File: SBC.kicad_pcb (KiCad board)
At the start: 4 copper layers, 85 x 54 mm, 283 parts, among them J1 USB_OTG, J2 DIN41612_02x10_AB, J3 USB_OTG, J4 Conn_02x20_Counter_Clockwise, J5 Conn_01x15_Socket, J6 Conn_01x06_Socket, SW1 SW_DIP_x03, U1 STPMIC1APQR, U2 IS43TR16640C-125JBL, U3 ECMF02-2AMX6, U4 ECMF02-2AMX6, U5 STM32MP157FADx, U6 IS21ES08GA-JQLI-TR, U7 LAN8720A, U8 ARJM11C7-114-BA-EW2, X1 ASE-24MHz, Y1 25MHz

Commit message: Layout started
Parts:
- removed R17: 680, Resistor_SMD:R_0402_1005Metric
- removed R18, R19, R20: 22, Resistor_SMD:R_0402_1005Metric
- removed R21, R22: 10k, Resistor_SMD:R_0402_1005Metric
- removed R23, R24: 1.5k, Resistor_SMD:R_0402_1005Metric
- removed R25: 3k, Resistor_SMD:R_0402_1005Metric
- added D10: Red, SparkFun-LED:LED_0603_1608Metric, F.Cu at (178.4, 70.3)
- added D11: Red, SparkFun-LED:LED_0603_1608Metric, F.Cu at (178.4, 72.8)
- added D12: Red, SparkFun-LED:LED_0603_1608Metric, F.Cu at (178.4, 75.3)
- added D13: Red, SparkFun-LED:LED_0603_1608Metric, F.Cu at (178.4, 77.8)
- added D14: Red, SparkFun-LED:LED_0603_1608Metric, F.Cu at (178.4, 80.3)
- added D15: Red, SparkFun-LED:LED_0603_1608Metric, F.Cu at (193.2, 76.4)
- added D16: Blue, SparkFun-LED:LED_0603_1608Metric, F.Cu at (193.2, 78.9)
- added D17: ECMF04-4HSWM10, footprints:QFN-10L_DTS, F.Cu at (106.0, 80.0)
- added D18: ECMF04-4HSWM10, footprints:QFN-10L_DTS, F.Cu at (197.5, 73.0)
- added D5: Red, SparkFun-LED:LED_0603_1608Metric, F.Cu at (53.0, 33.8)
- added D6: Red, SparkFun-LED:LED_0603_1608Metric, F.Cu at (178.4, 60.3)
- added D7: Red, SparkFun-LED:LED_0603_1608Metric, F.Cu at (178.4, 62.8)
- added D8: Red, SparkFun-LED:LED_0603_1608Metric, F.Cu at (178.4, 65.3)
- added D9: Red, SparkFun-LED:LED_0603_1608Metric, F.Cu at (178.4, 67.8)
- added R10: 680, Resistor_SMD:R_0402_1005Metric, F.Cu at (187.7, 62.0)
- added R11: 680, Resistor_SMD:R_0402_1005Metric, F.Cu at (187.7, 64.0)
- added R129: 75, Capacitor_SMD:C_0402_1005Metric, F.Cu at (52.5, 36.0)
- added R130: 75, Capacitor_SMD:C_0402_1005Metric, F.Cu at (192.6, 60.0)
- added R131: 75, Capacitor_SMD:C_0402_1005Metric, F.Cu at (192.6, 62.0)
- added R132: 75, Capacitor_SMD:C_0402_1005Metric, F.Cu at (192.6, 63.9)
- added R133: 4.75k, Capacitor_SMD:C_0402_1005Metric, F.Cu at (192.6, 65.9)
- added R134: 4.75k, Capacitor_SMD:C_0402_1005Metric, F.Cu at (192.6, 67.9)
- added R135: 4.75k, Capacitor_SMD:C_0402_1005Metric, F.Cu at (195.5, 60.0)
- added R136: 4.75k, Capacitor_SMD:C_0402_1005Metric, F.Cu at (195.5, 62.0)
- added R137: 4.75k, Capacitor_SMD:C_0402_1005Metric, F.Cu at (195.5, 63.9)
- added R138: 0, Capacitor_SMD:C_0402_1005Metric, F.Cu at (195.5, 65.9)
- added R139: 4.75k, Capacitor_SMD:C_0402_1005Metric, F.Cu at (195.5, 67.9)
- added R140: 4.75k, Capacitor_SMD:C_0402_1005Metric, F.Cu at (198.4, 60.0)
- added R141: 4.75k, Capacitor_SMD:C_0402_1005Metric, F.Cu at (198.4, 62.0)
- added R142: 4.75k, Capacitor_SMD:C_0402_1005Metric, F.Cu at (198.4, 63.9)
- added R3: 680, Resistor_SMD:R_0402_1005Metric, F.Cu at (181.9, 60.0)
- added R4: 680, Resistor_SMD:R_0402_1005Metric, F.Cu at (181.9, 62.0)
- added R5: 680, Resistor_SMD:R_0402_1005Metric, F.Cu at (181.9, 64.0)
- added R6: 680, Resistor_SMD:R_0402_1005Metric, F.Cu at (184.8, 60.0)
- added R7: 680, Resistor_SMD:R_0402_1005Metric, F.Cu at (184.8, 62.0)
- added R8: 680, Resistor_SMD:R_0402_1005Metric, F.Cu at (184.8, 64.0)
- added R9: 680, Resistor_SMD:R_0402_1005Metric, F.Cu at (187.7, 60.0)
- D2: value Blue -> Red
- D3, D4: value ECMF04-4HSWM10 -> Red; footprint footprints:QFN-10L_DTS -> SparkFun-LED:LED_0603_1608Metric
- R1, R2: value 1.5k -> 680; footprint SparkFun-Resistor:R_0603_1608Metric -> Resistor_SMD:R_0402_1005Metric
- R101, R102, R103, R114: footprint Capacitor_SMD:C_0402_1005Metric -> Resistor_SMD:R_0402_1005Metric
- R104, R105, R106, R107: value 49.9 -> 10k; footprint Capacitor_SMD:C_0402_1005Metric -> Resistor_SMD:R_0402_1005Metric
- R108, R109: value 270 -> 10k; footprint Capacitor_SMD:C_0402_1005Metric -> Resistor_SMD:R_0402_1005Metric
- R110: value 12.1k -> 10k; footprint Capacitor_SMD:C_0402_1005Metric -> Resistor_SMD:R_0402_1005Metric
- R111, R112, R113: value 0 -> 10k; footprint Capacitor_SMD:C_0402_1005Metric -> Resistor_SMD:R_0402_1005Metric
- R115, R116, R117: value 75 -> 10k
- R118: value 75 -> 49.9
- R119, R120, R121: value 4.75k -> 49.9
- R12: value 240 -> 1.5k; footprint Resistor_SMD:R_0402_1005Metric -> SparkFun-Resistor:R_0603_1608Metric
- R122, R123: value 4.75k -> 270
- R124: value 0 -> 12.1k
- R125, R126, R127: value 4.75k -> 0
- R128: value 4.75k -> 10k
- R13: value 100 -> 1.5k; footprint Resistor_SMD:R_0402_1005Metric -> SparkFun-Resistor:R_0603_1608Metric
- R14: value 1k -> 680
- R15: value 22 -> 680
- R26, R50: value 10k -> 240
- R27: value 22 -> 100
- R28: value 10 -> 1k
- R29, R32: value 0 -> 22
- R30: value 10k -> 680
- R31: value 0 -> 680
- R33: value 1k -> 22
- R34, R41: value 10k -> 22
- R36: value 240 -> 10k
- R37, R38: value 10k -> 1.5k
- R39: value 10k -> 3k
- R42: value 10k -> 10
- R43, R45, R46: value 10k -> 0
- R47: value 10k -> 1k
- moved U3 211.9 mm to (40.0, 50.5), turned to 180 degrees
- moved U4 210.6 mm to (40.0, 61.5), turned to 180 degrees
- moved U6 206.3 mm to (63.5, 66.0)
- moved SW2 198.8 mm to (55.5, 44.0)
- moved U2 187.9 mm to (79.2, 57.6), turned to -90 degrees
- moved J1 184.9 mm to (33.0, 51.0), turned to -90 degrees
- moved J3 184.4 mm to (33.0, 62.0), turned to -90 degrees
- moved U7 172.5 mm to (58.0, 84.0), turned to 90 degrees
- moved U1 172.5 mm to (79.5, 85.0)
- moved X1 166.0 mm to (89.0, 73.5)
- moved U8 163.1 mm to (46.5, 89.2), turned to 90 degrees
- moved U5 162.0 mm to (79.2, 71.0), turned to 90 degrees
- moved J6 154.3 mm to (99.2, 49.5), turned to 90 degrees
- moved J4 141.7 mm to (63.6, 45.0), turned to 90 degrees
- moved J5 137.9 mm to (107.9, 66.0), turned to 90 degrees
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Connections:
- D1 pad 2: VDD -> VIN
- D2 pad 2: VDD -> /MPU/VDDCORE
- D3 pad 1: Net-(J5-Pin_6) -> Net-(D3-K)
- D3 pad 2: Net-(J5-Pin_5) -> /MPU/VDD_DDR
- D4 pad 1: Net-(D4-D1+-Pad1) -> Net-(D4-K)
- D4 pad 2: Net-(D4-D1+-Pad1) -> VDD
- J4 pad 1: /MPU/PA3 -> VIN
- J4 pad 11: /MPU/PB12 -> GND
- J4 pad 20: /MPU/PC10 -> GND
- J4 pad 21: /MPU/PC11 -> GND
- J4 pad 30: /MPU/PD5 -> GND
- J4 pad 39: /MPU/PE0 -> GND
- J4 pad 40: /MPU/PE1 -> VIN
- R1 pad 1: /Power/VIO -> Net-(D1-K)
- R1 pad 2: /MPU/I2C_SCL -> GND
- R100 pad 1: /MPU/PD7 -> /MPU/PC8
- R101 pad 1: /NAND/VDD -> /MPU/PC9
- R101 pad 2: /MPU/SDMMC2_CMD -> GND
- R102 pad 1: /NAND/VDD -> /MPU/PC10
- R102 pad 2: /MPU/SDMMC2_CLK -> GND
- R103 pad 1: /NAND/VDD -> /MPU/PC11
- R103 pad 2: /MPU/SDMMC2_D0 -> GND
- R104 pad 1: /Ethernet/RXN -> /MPU/PC12
- R104 pad 2: /Ethernet/VDDA -> GND
- R105 pad 1: /Ethernet/RXP -> /MPU/PC13
- R105 pad 2: /Ethernet/VDDA -> GND
- R106 pad 1: /Ethernet/TXN -> /MPU/PC14
- R106 pad 2: /Ethernet/VDDA -> GND
- R107 pad 1: /Ethernet/TXP -> /MPU/PC15
- R107 pad 2: /Ethernet/VDDA -> GND
- R108 pad 1: GND -> /MPU/PD0
- R108 pad 2: /Ethernet/GREEN -> GND
- R109 pad 1: GND -> /MPU/PD1
- R109 pad 2: /Ethernet/YELLOW -> GND
- R110 pad 1: Net-(U7-RBIAS) -> /MPU/PD2
- R111 pad 1: /Ethernet/ETH_CLK -> /MPU/PD4
- R111 pad 2: Net-(U7-XTAL1/CLKIN) -> GND
- R112 pad 1: Net-(C73-Pad2) -> /MPU/PD5
- R112 pad 2: /Ethernet/ETH_CLK -> GND
- R113 pad 1: Net-(U7-XTAL2) -> /MPU/PD6
- R113 pad 2: Net-(C74-Pad2) -> GND
- R114 pad 1: /Ethernet/LED2 -> /MPU/PD7
- R115 pad 1: Net-(C76-Pad1) -> /NAND/VDD
- R115 pad 2: Net-(U8-VC2-) -> /MPU/SDMMC2_CMD
- R116 pad 1: Net-(C77-Pad1) -> /NAND/VDD
- R116 pad 2: Net-(U8-VC1-) -> /MPU/SDMMC2_CLK
- R117 pad 1: Net-(C78-Pad1) -> /NAND/VDD
- R117 pad 2: Net-(U8-VC2+) -> /MPU/SDMMC2_D0
- R118 pad 1: Net-(C79-Pad1) -> /Ethernet/RXN
- R118 pad 2: Net-(U8-VC1+) -> /Ethernet/VDDA
- R119 pad 1: /Ethernet/PHYADDR -> /Ethernet/RXP
- R119 pad 2: VDD -> /Ethernet/VDDA
- R12 pad 1: /Memory/ZQ -> /Power/VIO
- R12 pad 2: GND -> /MPU/I2C_SCL
- R120 pad 1: /Ethernet/MODE0 -> /Ethernet/TXN
- R120 pad 2: VDD -> /Ethernet/VDDA
- R121 pad 1: /Ethernet/MODE1 -> /Ethernet/TXP
- R121 pad 2: VDD -> /Ethernet/VDDA
- R122 pad 1: /Ethernet/MODE2 -> GND
- R122 pad 2: VDD -> /Ethernet/GREEN
- R123 pad 1: /MPU/ETH1_RMII_REF_CLK -> GND
- R123 pad 2: VDD -> /Ethernet/YELLOW
- R124 pad 1: /Ethernet/REFCLKO -> Net-(U7-RBIAS)
- R124 pad 2: /MPU/ETH1_RMII_REF_CLK -> GND
- R125 pad 1: GND -> /Ethernet/ETH_CLK
- R125 pad 2: /Ethernet/PHYADDR -> Net-(U7-XTAL1/CLKIN)
- R126 pad 1: GND -> Net-(C73-Pad2)
- R126 pad 2: /Ethernet/MODE0 -> /Ethernet/ETH_CLK
- R127 pad 1: GND -> Net-(U7-XTAL2)
- R127 pad 2: /Ethernet/MODE1 -> Net-(C74-Pad2)
- R128 pad 1: GND -> /Ethernet/LED2
- R128 pad 2: /Ethernet/MODE2 -> GND
- R13 pad 1: /MPU/DDR_CLKP -> /Power/VIO
- R13 pad 2: /MPU/DDR_CLKN -> /MPU/I2C_SDA
- R14 pad 1: VDD -> Net-(D12-K)
- R14 pad 2: Net-(R14-Pad2) -> GND
- R15 pad 1: /MPU/ETH_CLK_R -> Net-(D13-K)
- R15 pad 2: /Ethernet/ETH_CLK -> GND
- R16 pad 1: /MPU/DBGRQ -> Net-(D14-K)
- R16 pad 2: Net-(D2-K) -> GND
- R2 pad 1: /Power/VIO -> Net-(D2-K)
- R2 pad 2: /MPU/I2C_SDA -> GND
- R26 pad 1: GND -> /Memory/ZQ
- R26 pad 2: Net-(J2-Pin_a6) -> GND
- R27 pad 1: /MPU/ETH1_MDC_R -> /MPU/DDR_CLKP
- R27 pad 2: /Ethernet/MDC -> /MPU/DDR_CLKN
- R28 pad 2: Net-(X1-Vdd) -> Net-(R28-Pad2)
- R29 pad 1: Net-(U5-DDR_DTO1) -> /MPU/ETH_CLK_R
- R29 pad 2: GND -> /Ethernet/ETH_CLK
- R30 pad 1: VDD -> /MPU/DBGRQ
- R30 pad 2: Net-(X1-EN) -> Net-(D16-K)
- R31 pad 1: Net-(U5-DDR_DTO0) -> /MPU/DBGACK
- R31 pad 2: GND -> Net-(D15-K)
- R32 pad 1: /MPU/OSC_OUT -> /MPU/ETH1_RMII_TX_EN_R
- R32 pad 2: Net-(X1-EN) -> /Ethernet/TXEN
- R33 pad 1: GND -> /MPU/ETH1_RMII_TXD1_R
- R33 pad 2: /MPU/OSC_OUT -> /Ethernet/TXD1
- R34 pad 1: /MPU/DDR_RESETn -> /MPU/ETH1_RMII_TXD0_R
- R34 pad 2: GND -> /Ethernet/TXD0
- R35 pad 1: /MPU/DDR_CKE -> GND
- R35 pad 2: GND -> /MPU/DBGACK
- R36 pad 1: /MPU/ZQ -> GND
- R36 pad 2: GND -> /MPU/DBGRQ
- R37 pad 1: Net-(D4-D1+-Pad10) -> /Ethernet/MDC
- R37 pad 2: GND -> VDD
- R38 pad 1: Net-(D4-D1+-Pad1) -> /MPU/ETH1_MDIO
- R38 pad 2: GND -> VDD
- R39 pad 1: /MPU/PD8 -> /MPU/USB_RREF
- R40 pad 1: /MPU/PD9 -> GND
- R40 pad 2: GND -> Net-(J2-Pin_a6)
- R41 pad 1: /MPU/PD10 -> /MPU/ETH1_MDC_R
- R41 pad 2: GND -> /Ethernet/MDC
- R42 pad 1: /MPU/PD11 -> VDD
- R42 pad 2: GND -> Net-(X1-Vdd)
- R43 pad 1: /MPU/PD14 -> Net-(U5-DDR_DTO1)
- R44 pad 1: /MPU/PD15 -> VDD
- R44 pad 2: GND -> Net-(X1-EN)
- R45 pad 1: /MPU/PE0 -> Net-(U5-DDR_DTO0)
- R46 pad 1: /MPU/PE1 -> /MPU/OSC_OUT
- R46 pad 2: GND -> Net-(X1-EN)
- R47 pad 1: /MPU/PE2 -> GND
- R47 pad 2: GND -> /MPU/OSC_OUT
- R48 pad 1: /MPU/PE4 -> /MPU/DDR_RESETn
- R49 pad 1: /MPU/PE6 -> /MPU/DDR_CKE
- R50 pad 1: /MPU/PE7 -> /MPU/ZQ
- R51 pad 1: /MPU/PE8 -> Net-(D18-D1+-Pad10)
- R52 pad 1: /MPU/PE9 -> Net-(D18-D1+-Pad1)
- R53 pad 1: /MPU/PE10 -> /MPU/PD8
- R54 pad 1: /MPU/PE11 -> /MPU/PD9
- R55 pad 1: /MPU/PE12 -> /MPU/PD10
- R56 pad 1: /MPU/PE13 -> /MPU/PD11
- R57 pad 1: /MPU/PE14 -> /MPU/PD14
- R58 pad 1: /MPU/PE15 -> /MPU/PD15
- R59 pad 1: /MPU/PF6 -> /MPU/PE0
- R60 pad 1: /MPU/PF7 -> /MPU/PE1
- R61 pad 1: /MPU/PF8 -> /MPU/PE2
- R62 pad 1: /MPU/PF9 -> /MPU/PE4
- R63 pad 1: /MPU/PF10 -> /MPU/PE6
- R64 pad 1: /MPU/PF11 -> /MPU/PE7
- R65 pad 1: /MPU/PG7 -> /MPU/PE8
- R66 pad 1: /MPU/PG9 -> /MPU/PE9
- R67 pad 1: /MPU/PG10 -> /MPU/PE10
- R68 pad 1: /MPU/PG15 -> /MPU/PE11
- R69 pad 1: /MPU/PA3 -> /MPU/PE12
- R70 pad 1: /MPU/PA4 -> /MPU/PE13
- R71 pad 1: /MPU/PA5 -> /MPU/PE14
- R72 pad 1: /MPU/PA6 -> /MPU/PE15
- R73 pad 1: /MPU/PA8 -> /MPU/PF6
- R74 pad 1: /MPU/PA9 -> /MPU/PF7
- R75 pad 1: /MPU/PB1 -> /MPU/PF8
- R76 pad 1: /MPU/PB5 -> /MPU/PF9
- R77 pad 1: /MPU/PB6 -> /MPU/PF10
- R78 pad 1: /MPU/PB7 -> /MPU/PF11
- R79 pad 1: /MPU/PB12 -> /MPU/PG7
- R80 pad 1: /MPU/PB13 -> /MPU/PG9
- R81 pad 1: /MPU/PC0 -> /MPU/PG10
- R82 pad 1: /MPU/PC2 -> /MPU/PG15
- R83 pad 1: /MPU/PC3 -> /MPU/PA3
- R84 pad 1: /MPU/PC6 -> /MPU/PA4
- R85 pad 1: /MPU/PC7 -> /MPU/PA5
- R86 pad 1: /MPU/PC8 -> /MPU/PA6
- R87 pad 1: /MPU/PC9 -> /MPU/PA8
- R88 pad 1: /MPU/PC10 -> /MPU/PA9
- R89 pad 1: /MPU/PC11 -> /MPU/PB1
- R90 pad 1: /MPU/PC12 -> /MPU/PB5
- R91 pad 1: /MPU/PC13 -> /MPU/PB6
- R92 pad 1: /MPU/PC14 -> /MPU/PB7
- R93 pad 1: /MPU/PC15 -> /MPU/PB12
- R94 pad 1: /MPU/PD0 -> /MPU/PB13
- R95 pad 1: /MPU/PD1 -> /MPU/PC0
- R96 pad 1: /MPU/PD2 -> /MPU/PC2
- R97 pad 1: /MPU/PD4 -> /MPU/PC3
- R98 pad 1: /MPU/PD5 -> /MPU/PC6
- R99 pad 1: /MPU/PD6 -> /MPU/PC7
- SW1 pad 4: Net-(R14-Pad2) -> Net-(R28-Pad2)
- SW1 pad 5: Net-(R14-Pad2) -> Net-(R28-Pad2)
- SW1 pad 6: Net-(R14-Pad2) -> Net-(R28-Pad2)
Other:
- board size 85 x 54 mm -> 85 x 73 mm
- copper layers 4 -> 6

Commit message: Component placement
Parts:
- removed SW2: ~, SparkFun-Switch:Push_SMD_4.2x3.2mm
- added H1: MountingHole, MountingHole:MountingHole_3.2mm_M3, F.Cu at (34.0, 44.0)
- added H2: MountingHole, MountingHole:MountingHole_3.2mm_M3, F.Cu at (34.0, 90.0)
- added H3: MountingHole, MountingHole:MountingHole_3.2mm_M3, F.Cu at (111.0, 44.0)
- added H4: MountingHole, MountingHole:MountingHole_3.2mm_M3, F.Cu at (111.0, 90.0)
- added JP1: SolderJumper_2_Open, SparkFun-Jumper:Jumper_2_NO, F.Cu at (111.0, 76.5)
- added JP2: SolderJumper_2_Open, SparkFun-Jumper:Jumper_2_NO, F.Cu at (111.0, 78.9)
- added JP3: SolderJumper_2_Open, SparkFun-Jumper:Jumper_2_NO, F.Cu at (111.0, 81.4)
- added R143: 4.75k, Capacitor_SMD:C_0402_1005Metric, F.Cu at (120.3, 82.8)
- added R144: 4.75k, Capacitor_SMD:C_0402_1005Metric, F.Cu at (120.3, 84.8)
- added TP22: RCWCTE, footprints:TP420X150, F.Cu at (94.0, 92.0)
- added TP23: RCWCTE, footprints:TP420X150, F.Cu at (101.5, 92.0)
- R115, R116: footprint Capacitor_SMD:C_0402_1005Metric -> Resistor_SMD:R_0402_1005Metric
- R118, R119: value 49.9 -> 10k
- R12: footprint SparkFun-Resistor:R_0603_1608Metric -> Resistor_SMD:R_0402_1005Metric
- R122, R123: value 270 -> 49.9
- R124: value 12.1k -> 270
- R125: value 0 -> 270
- R126: value 0 -> 12.1k
- R128, R48: value 10k -> 0
- R129: value 75 -> 0
- R13: footprint SparkFun-Resistor:R_0603_1608Metric -> LED_SMD:LED_0402_1005Metric
- R130: value 75 -> 10k
- R133, R134: value 4.75k -> 75
- R138: value 0 -> 4.75k
- R140: value 4.75k -> 0
- R29: value 22 -> 1k
- R30: value 680 -> 1k
- R31: value 680 -> 22
- R32, R33: value 22 -> 680
- R35, R36: value 10k -> 22
- R37, R38: value 1.5k -> 10k
- R39: value 3k -> 1.5k
- R40: value 10k -> 1.5k
- R41: value 22 -> 3k
- R42: value 10 -> 10k
- R43: value 0 -> 22
- R44: value 10k -> 10
- R46: value 0 -> 10k
- R47: value 1k -> 0
- R49: value 10k -> 1k
- R50: value 240 -> 10k
- R52: value 10k -> 240
- SW1: value SW_DIP_x03 -> ~; footprint Button_Switch_SMD:SW_DIP_SPSTx03_Slide_9.78x9.8mm_W8.61mm_P2.54mm -> SparkFun-Switch:Push_SMD_4.2x3.2mm
- moved CR4 187.2 mm to (69.0, 81.5), turned to -90 degrees
- moved CR3 181.7 mm to (75.5, 81.5), turned to -90 degrees
- moved CR9 181.3 mm to (56.4, 76.3)
- moved D1 171.2 mm to (88.5, 88.0), turned to 90 degrees
- moved D2 167.8 mm to (91.5, 88.0), turned to 90 degrees
- moved Y1 155.8 mm to (89.0, 70.5)
- moved LX4 152.7 mm to (92.5, 83.5)
- moved LX2 151.9 mm to (92.5, 80.5)
- moved CR8 150.0 mm to (103.0, 54.0), turned to 90 degrees
- moved R32 144.5 mm to (70.0, 74.5), turned to 90 degrees
- moved LXB1 143.7 mm to (103.5, 79.0), turned to 180 degrees
- moved R33 143.5 mm to (71.0, 74.5), turned to 90 degrees
- moved LX3 140.9 mm to (103.5, 85.0)
- moved LX1 140.2 mm to (103.5, 82.0)
- moved D4 136.0 mm to (90.0, 88.0), turned to 90 degrees
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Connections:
- R100 pad 1: /MPU/PC8 -> /MPU/PC6
- R101 pad 1: /MPU/PC9 -> /MPU/PC7
- R102 pad 1: /MPU/PC10 -> /MPU/PC8
- R103 pad 1: /MPU/PC11 -> /MPU/PC9
- R104 pad 1: /MPU/PC12 -> /MPU/PC10
- R105 pad 1: /MPU/PC13 -> /MPU/PC11
- R106 pad 1: /MPU/PC14 -> /MPU/PC12
- R107 pad 1: /MPU/PC15 -> /MPU/PC13
- R108 pad 1: /MPU/PD0 -> /MPU/PC14
- R109 pad 1: /MPU/PD1 -> /MPU/PC15
- R110 pad 1: /MPU/PD2 -> /MPU/PD0
- R111 pad 1: /MPU/PD4 -> /MPU/PD1
- R112 pad 1: /MPU/PD5 -> /MPU/PD2
- R113 pad 1: /MPU/PD6 -> /MPU/PD4
- R114 pad 1: /MPU/PD7 -> /MPU/PD5
- R115 pad 1: /NAND/VDD -> /MPU/PD6
- R115 pad 2: /MPU/SDMMC2_CMD -> GND
- R116 pad 1: /NAND/VDD -> /MPU/PD7
- R116 pad 2: /MPU/SDMMC2_CLK -> GND
- R117 pad 2: /MPU/SDMMC2_D0 -> /MPU/SDMMC2_CMD
- R118 pad 1: /Ethernet/RXN -> /NAND/VDD
- R118 pad 2: /Ethernet/VDDA -> /MPU/SDMMC2_CLK
- R119 pad 1: /Ethernet/RXP -> /NAND/VDD
- R119 pad 2: /Ethernet/VDDA -> /MPU/SDMMC2_D0
- R120 pad 1: /Ethernet/TXN -> /Ethernet/RXN
- R121 pad 1: /Ethernet/TXP -> /Ethernet/RXP
- R122 pad 1: GND -> /Ethernet/TXN
- R122 pad 2: /Ethernet/GREEN -> /Ethernet/VDDA
- R123 pad 1: GND -> /Ethernet/TXP
- R123 pad 2: /Ethernet/YELLOW -> /Ethernet/VDDA
- R124 pad 1: Net-(U7-RBIAS) -> GND
- R124 pad 2: GND -> /Ethernet/GREEN
- R125 pad 1: /Ethernet/ETH_CLK -> GND
- R125 pad 2: Net-(U7-XTAL1/CLKIN) -> /Ethernet/YELLOW
- R126 pad 1: Net-(C73-Pad2) -> Net-(U7-RBIAS)
- R126 pad 2: /Ethernet/ETH_CLK -> GND
- R127 pad 1: Net-(U7-XTAL2) -> /Ethernet/ETH_CLK
- R127 pad 2: Net-(C74-Pad2) -> Net-(U7-XTAL1/CLKIN)
- R128 pad 1: /Ethernet/LED2 -> Net-(C73-Pad2)
- R128 pad 2: GND -> /Ethernet/ETH_CLK
- R129 pad 1: Net-(C76-Pad1) -> Net-(U7-XTAL2)
- R129 pad 2: Net-(U8-VC2-) -> Net-(C74-Pad2)
- R130 pad 1: Net-(C77-Pad1) -> /Ethernet/LED2
- R130 pad 2: Net-(U8-VC1-) -> GND
- R131 pad 1: Net-(C78-Pad1) -> Net-(C76-Pad1)
- R131 pad 2: Net-(U8-VC2+) -> Net-(U8-VC2-)
- R132 pad 1: Net-(C79-Pad1) -> Net-(C77-Pad1)
- R132 pad 2: Net-(U8-VC1+) -> Net-(U8-VC1-)
- R133 pad 1: /Ethernet/PHYADDR -> Net-(C78-Pad1)
- R133 pad 2: VDD -> Net-(U8-VC2+)
- R134 pad 1: /Ethernet/MODE0 -> Net-(C79-Pad1)
- R134 pad 2: VDD -> Net-(U8-VC1+)
- R135 pad 1: /Ethernet/MODE1 -> /Ethernet/PHYADDR
- R136 pad 1: /Ethernet/MODE2 -> /Ethernet/MODE0
- R137 pad 1: /MPU/ETH1_RMII_REF_CLK -> /Ethernet/MODE1
- R138 pad 1: /Ethernet/REFCLKO -> /Ethernet/MODE2
- R138 pad 2: /MPU/ETH1_RMII_REF_CLK -> VDD
- R139 pad 1: GND -> /MPU/ETH1_RMII_REF_CLK
- R139 pad 2: /Ethernet/PHYADDR -> VDD
- R140 pad 1: GND -> /Ethernet/REFCLKO
- R140 pad 2: /Ethernet/MODE0 -> /MPU/ETH1_RMII_REF_CLK
- R141 pad 2: /Ethernet/MODE1 -> /Ethernet/PHYADDR
- R142 pad 2: /Ethernet/MODE2 -> /Ethernet/MODE0
- R28 pad 2: Net-(R28-Pad2) -> Net-(JP1-B)
- R29 pad 1: /MPU/ETH_CLK_R -> VDD
- R29 pad 2: /Ethernet/ETH_CLK -> Net-(JP2-B)
- R30 pad 1: /MPU/DBGRQ -> VDD
- R30 pad 2: Net-(D16-K) -> Net-(JP3-B)
- R31 pad 1: /MPU/DBGACK -> /MPU/ETH_CLK_R
- R31 pad 2: Net-(D15-K) -> /Ethernet/ETH_CLK
- R32 pad 1: /MPU/ETH1_RMII_TX_EN_R -> /MPU/DBGRQ
- R32 pad 2: /Ethernet/TXEN -> Net-(D16-K)
- R33 pad 1: /MPU/ETH1_RMII_TXD1_R -> /MPU/DBGACK
- R33 pad 2: /Ethernet/TXD1 -> Net-(D15-K)
- R34 pad 1: /MPU/ETH1_RMII_TXD0_R -> /MPU/ETH1_RMII_TX_EN_R
- R34 pad 2: /Ethernet/TXD0 -> /Ethernet/TXEN
- R35 pad 1: GND -> /MPU/ETH1_RMII_TXD1_R
- R35 pad 2: /MPU/DBGACK -> /Ethernet/TXD1
- R36 pad 1: GND -> /MPU/ETH1_RMII_TXD0_R
- R36 pad 2: /MPU/DBGRQ -> /Ethernet/TXD0
- R37 pad 1: /Ethernet/MDC -> GND
- R37 pad 2: VDD -> /MPU/DBGACK
- R38 pad 1: /MPU/ETH1_MDIO -> GND
- R38 pad 2: VDD -> /MPU/DBGRQ
- R39 pad 1: /MPU/USB_RREF -> /Ethernet/MDC
- R39 pad 2: GND -> VDD
- R40 pad 1: GND -> /MPU/ETH1_MDIO
- R40 pad 2: Net-(J2-Pin_a6) -> VDD
- R41 pad 1: /MPU/ETH1_MDC_R -> /MPU/USB_RREF
- R41 pad 2: /Ethernet/MDC -> GND
- R42 pad 1: VDD -> GND
- R42 pad 2: Net-(X1-Vdd) -> Net-(J2-Pin_a6)
- R43 pad 1: Net-(U5-DDR_DTO1) -> /MPU/ETH1_MDC_R
- R43 pad 2: GND -> /Ethernet/MDC
- R44 pad 2: Net-(X1-EN) -> Net-(X1-Vdd)
- R45 pad 1: Net-(U5-DDR_DTO0) -> Net-(U5-DDR_DTO1)
- R46 pad 1: /MPU/OSC_OUT -> VDD
- R47 pad 1: GND -> Net-(U5-DDR_DTO0)
- R47 pad 2: /MPU/OSC_OUT -> GND
- R48 pad 1: /MPU/DDR_RESETn -> /MPU/OSC_OUT
- R48 pad 2: GND -> Net-(X1-EN)
- R49 pad 1: /MPU/DDR_CKE -> GND
- R49 pad 2: GND -> /MPU/OSC_OUT
- R50 pad 1: /MPU/ZQ -> /MPU/DDR_RESETn
- R51 pad 1: Net-(D18-D1+-Pad10) -> /MPU/DDR_CKE
- R52 pad 1: Net-(D18-D1+-Pad1) -> /MPU/ZQ
- R53 pad 1: /MPU/PD8 -> Net-(D18-D1+-Pad10)
- R54 pad 1: /MPU/PD9 -> Net-(D18-D1+-Pad1)
- R55 pad 1: /MPU/PD10 -> /MPU/PD8
- R56 pad 1: /MPU/PD11 -> /MPU/PD9
- R57 pad 1: /MPU/PD14 -> /MPU/PD10
- R58 pad 1: /MPU/PD15 -> /MPU/PD11
- R59 pad 1: /MPU/PE0 -> /MPU/PD14
- R60 pad 1: /MPU/PE1 -> /MPU/PD15
- R61 pad 1: /MPU/PE2 -> /MPU/PE0
- R62 pad 1: /MPU/PE4 -> /MPU/PE1
- R63 pad 1: /MPU/PE6 -> /MPU/PE2
- R64 pad 1: /MPU/PE7 -> /MPU/PE4
- R65 pad 1: /MPU/PE8 -> /MPU/PE6
- R66 pad 1: /MPU/PE9 -> /MPU/PE7
- R67 pad 1: /MPU/PE10 -> /MPU/PE8
- R68 pad 1: /MPU/PE11 -> /MPU/PE9
- R69 pad 1: /MPU/PE12 -> /MPU/PE10
- R70 pad 1: /MPU/PE13 -> /MPU/PE11
- R71 pad 1: /MPU/PE14 -> /MPU/PE12
- R72 pad 1: /MPU/PE15 -> /MPU/PE13
- R73 pad 1: /MPU/PF6 -> /MPU/PE14
- R74 pad 1: /MPU/PF7 -> /MPU/PE15
- R75 pad 1: /MPU/PF8 -> /MPU/PF6
- R76 pad 1: /MPU/PF9 -> /MPU/PF7
- R77 pad 1: /MPU/PF10 -> /MPU/PF8
- R78 pad 1: /MPU/PF11 -> /MPU/PF9
- R79 pad 1: /MPU/PG7 -> /MPU/PF10
- R80 pad 1: /MPU/PG9 -> /MPU/PF11
- R81 pad 1: /MPU/PG10 -> /MPU/PG7
- R82 pad 1: /MPU/PG15 -> /MPU/PG9
- R83 pad 1: /MPU/PA3 -> /MPU/PG10
- R84 pad 1: /MPU/PA4 -> /MPU/PG15
- R85 pad 1: /MPU/PA5 -> /MPU/PA3
- R86 pad 1: /MPU/PA6 -> /MPU/PA4
- R87 pad 1: /MPU/PA8 -> /MPU/PA5
- R88 pad 1: /MPU/PA9 -> /MPU/PA6
- R89 pad 1: /MPU/PB1 -> /MPU/PA8
- R90 pad 1: /MPU/PB5 -> /MPU/PA9
- R91 pad 1: /MPU/PB6 -> /MPU/PB1
- R92 pad 1: /MPU/PB7 -> /MPU/PB5
- R93 pad 1: /MPU/PB12 -> /MPU/PB6
- R94 pad 1: /MPU/PB13 -> /MPU/PB7
- R95 pad 1: /MPU/PC0 -> /MPU/PB12
- R96 pad 1: /MPU/PC2 -> /MPU/PB13
- R97 pad 1: /MPU/PC3 -> /MPU/PC0
- R98 pad 1: /MPU/PC6 -> /MPU/PC2
- R99 pad 1: /MPU/PC7 -> /MPU/PC3
- SW1 pad 1: /MPU/BOOT0 -> GND
- SW1 pad 2: /MPU/BOOT1 -> /MPU/nRST
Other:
- board size 85 x 73 mm -> 85 x 54 mm

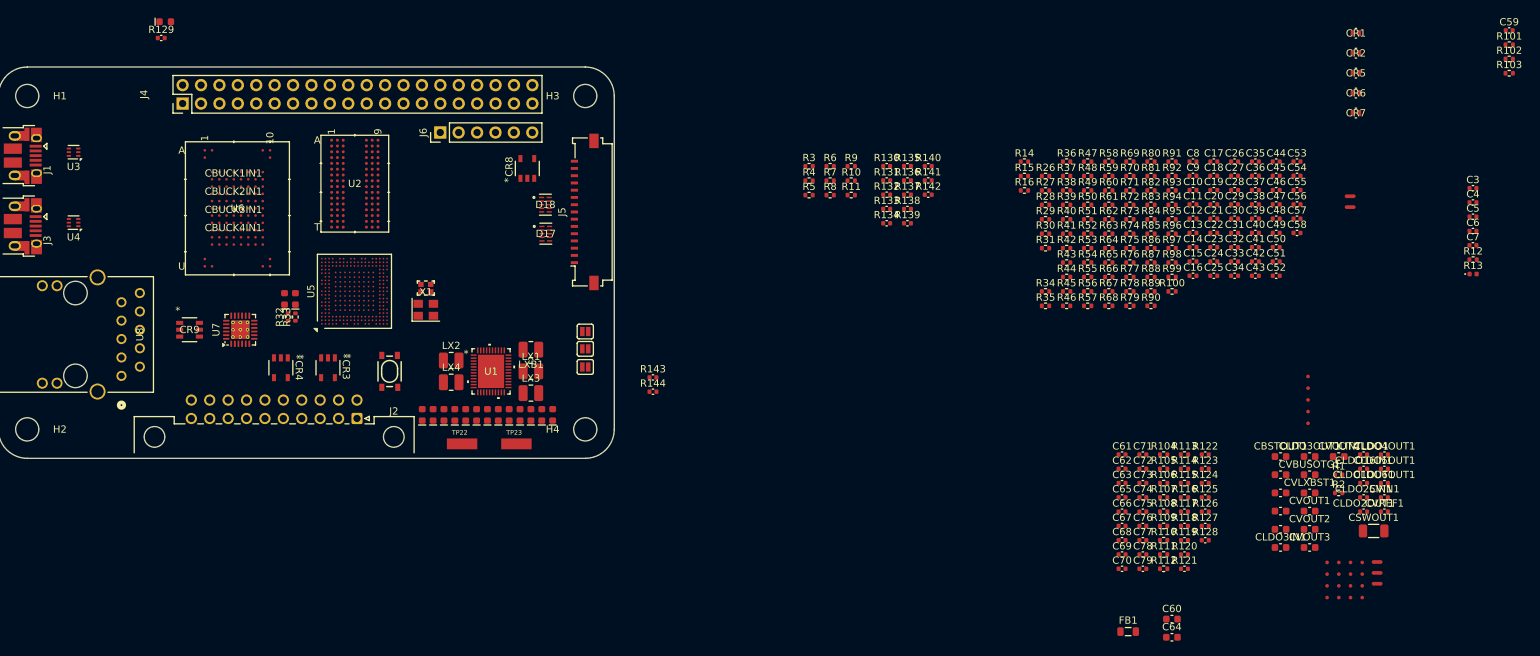
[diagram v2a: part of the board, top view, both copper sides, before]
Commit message: Roughly placed all components
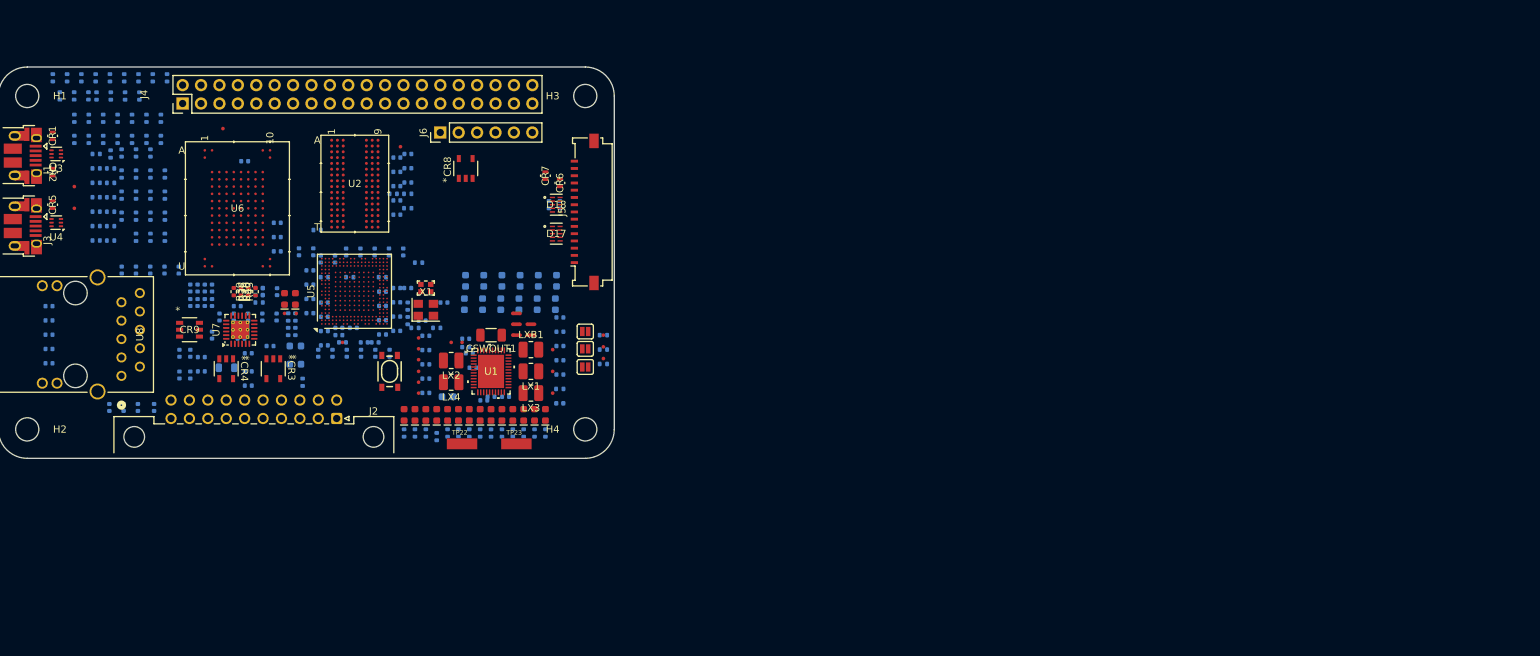
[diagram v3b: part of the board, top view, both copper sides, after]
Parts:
- C10, C11, C12, C13, C14, C15, C16, C17, C18, C19, C20, C21, C22, C23, C24, C25, C26, C27, C28, C29, C3, C30, C31, C32, C33, C34, C35, C36, C37, C38, C39, C4, C40, C41, C42, C43, C44, C45, C46, C47, C48, C49, C5, C50, C51, C52, C53, C54, C55, C56, C57, C58, C59, C6, C60, C61, C62, C63, C64, C65, C66, C67, C68, C69, C7, C70, C71, C72, C73, C74, C75, C76, C77, C78, C79, C8, C9, CBSTOUT1, CBUCK1IN1, CBUCK2IN1, CBUCK3IN1, CBUCK4IN1, CINTLDO1, CLDO16IN1, CLDO1OUT1, CLDO25IN1, CLDO2OUT1, CLDO3IN1, CLDO3OUT1, CLDO4OUT1, CLDO5OUT1, CLDO6OUT1, CVBUSOTG1, CVIN1, CVLXBST1, CVOUT1, CVOUT2, CVOUT3, CVOUT4, CVREF1, FB1, R1, R10, R100, R101, R102, R103, R104, R105, R106, R107, R108, R109, R11, R110, R111, R112, R113, R114, R115, R116, R117, R118, R119, R12, R120, R121, R122, R123, R124, R125, R126, R127, R128, R129, R13, R130, R131, R132, R133, R134, R135, R136, R137, R138, R139, R14, R140, R141, R142, R143, R144, R15, R16, R2, R26, R27, R28, R29, R3, R30, R31, R32, R33, R34, R35, R37, R38, R4, R41, R42, R44, R45, R46, R47, R48, R49, R5, R50, R51, R52, R53, R54, R55, R56, R57, R58, R59, R6, R60, R61, R62, R63, R64, R65, R66, R67, R68, R69, R7, R70, R71, R72, R73, R74, R75, R76, R77, R78, R79, R8, R80, R81, R82, R83, R84, R85, R86, R87, R88, R89, R9, R90, R91, R92, R93, R94, R95, R96, R97, R98, R99: moved to B.Cu
- moved R101 200.1 mm to (38.5, 44.0), turned to -90 degrees
- moved R102 198.1 mm to (40.5, 44.0), turned to -90 degrees
- moved R103 196.1 mm to (42.4, 44.0), turned to -90 degrees
- moved TP2 180.9 mm to (40.5, 56.5)
- moved CR5 180.8 mm to (37.5, 59.0), turned to 90 degrees
- moved CR2 180.6 mm to (37.5, 54.5), turned to -90 degrees
- moved TP3 180.5 mm to (40.5, 59.5)
- moved CR1 180.4 mm to (37.5, 49.5), turned to 90 degrees
- moved C59 175.4 mm to (64.0, 53.0), turned to 180 degrees
- moved R112 167.6 mm to (37.5, 41.5), turned to 90 degrees
- moved TP5 165.2 mm to (61.0, 48.5)
- moved R111 165.0 mm to (39.5, 41.5), turned to 90 degrees
- moved R110 162.4 mm to (41.5, 41.5), turned to 90 degrees
- moved R122 160.9 mm to (37.0, 73.0), turned to 180 degrees
- moved R123 160.9 mm to (37.0, 75.0), turned to 180 degrees
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
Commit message: Added notes
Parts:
- J2: footprint Connector_DIN:DIN41612_B3_2x10_Male_Horizontal_THT -> Connector_DIN:DIN41612_Q3_2x10_Male_Vertical_THT
- moved C14 18.0 mm to (78.3, 72.8)
- moved J2 11.5 mm to (75.2, 99.9), turned to -90 degrees
- moved CR3 9.28 mm to (67.4, 90.9)
- moved CR4 9.28 mm to (60.9, 90.9)
- moved J6 0.34 mm to (91.0, 48.7)
- moved CSWOUT1 0.10 mm to (98.0, 77.1)
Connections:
- C59 pad 1: unconnected-(C59-Pad1) -> /NAND/VDDI
- C59 pad 2: unconnected-(C59-Pad2) -> GND

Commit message: Added some routing, updated constraints and added net classes
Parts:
- moved R109 18.6 mm to (55.0, 56.0)
- moved R108 16.9 mm to (54.0, 56.0)
- moved R107 15.6 mm to (53.0, 56.0)
- moved R74 15.2 mm to (55.0, 52.0), turned to 90 degrees
- moved R104 14.9 mm to (50.0, 56.0)
- moved R106 14.8 mm to (52.0, 56.0)
- moved R101 14.7 mm to (47.0, 56.0), turned to 90 degrees
- moved R105 14.5 mm to (51.0, 56.0)
- moved R102 14.2 mm to (48.0, 56.0), turned to 90 degrees
- moved R75 14.2 mm to (46.0, 50.0), turned to 90 degrees
- moved R97 13.7 mm to (42.0, 56.0)
- moved R103 13.7 mm to (49.0, 56.0), turned to 90 degrees
- moved R112 13.3 mm to (42.0, 54.0)
- moved R73 13.2 mm to (54.0, 52.0), turned to 90 degrees
- moved R86 13.1 mm to (44.0, 60.0)
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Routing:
- net /DQ6: track 0.00 -> 1.04 mm, vias 0 -> 1
- net unconnected-(U5-PWR_LP-PadK1): vias 0 -> 1
- net unconnected-(U5-DDR_ATO-Pad1F8): vias 0 -> 1
- net VSSA: vias 0 -> 1
- net VDD: vias 0 -> 8
- net Net-(U5-DDR_DTO1): vias 0 -> 1
- net Net-(U5-DDR_DTO0): vias 0 -> 1
- net GND: vias 0 -> 43
- net /Power/INTn: vias 0 -> 1
- net /Memory/WEn: vias 0 -> 1
- net /Memory/RASn: vias 0 -> 1
- net /Memory/ODT: vias 0 -> 1
- net /Memory/CSn: vias 0 -> 1
- net /Memory/CASn: vias 0 -> 1
- net /MPU/nTRST: vias 0 -> 1
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
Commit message: minor changes
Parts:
- moved J2 23.9 mm to (73.9, 87.0)
- moved J1 15.3 mm to (46.0, 43.5), turned to 180 degrees
- moved U2 12.6 mm to (91.5, 59.0), turned to 0 degrees
- moved U5 11.5 mm to (79.7, 59.5), turned to 0 degrees
- moved CR1 11.4 mm to (48.8, 47.6), turned to 0 degrees
- moved CR2 9.31 mm to (43.8, 47.6), turned to 180 degrees
- moved U3 9.13 mm to (46.3, 48.1), turned to 90 degrees
- moved NT1 7.36 mm to (102.4, 66.7)
- moved NT2 7.36 mm to (102.4, 68.2)
- moved NT3 7.36 mm to (102.4, 69.7)
- moved NT4 7.36 mm to (104.4, 68.2)
- moved NT5 7.36 mm to (104.4, 69.7)
- moved CR5 6.98 mm to (37.6, 52.0)
- moved J3 6.98 mm to (33.5, 55.0)
- moved TP3 6.98 mm to (40.6, 52.5)
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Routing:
- net Net-(D9-K): track 0.00 -> 2.50 mm, vias 0 -> 1
- net Net-(D8-K): track 0.00 -> 2.50 mm, vias 0 -> 1
- net Net-(D7-K): track 0.00 -> 2.50 mm, vias 0 -> 1
- net Net-(D6-K): track 0.00 -> 2.50 mm, vias 0 -> 1
- net Net-(D5-K): track 0.00 -> 2.50 mm, vias 0 -> 1
- net Net-(D4-K): track 0.00 -> 2.50 mm, vias 0 -> 1
- net Net-(D3-K): track 0.00 -> 2.50 mm, vias 0 -> 1
- net Net-(D2-K): track 0.00 -> 2.50 mm, vias 0 -> 1
- net Net-(D14-K): track 0.00 -> 2.50 mm, vias 0 -> 1
- net Net-(D13-K): track 0.00 -> 2.50 mm, vias 0 -> 1
- net Net-(D12-K): track 0.00 -> 2.50 mm, vias 0 -> 1
- net Net-(D11-K): track 0.00 -> 2.50 mm, vias 0 -> 1
- net Net-(D10-K): track 0.00 -> 2.50 mm, vias 0 -> 1
- net Net-(D1-K): track 0.00 -> 2.50 mm, vias 0 -> 1
- net /MPU/VBUS_HOST: track 0.00 -> 1.63 mm
- added copper zone on F.Cu, net /MPU/VDD_DDR
- added copper zone on F.Cu, net /Power/VLX2
- added copper zone on B.Cu, net GND
- added copper zone on F.Cu, net GND
- added copper zone on In1.Cu, net GND
- added copper zone on In2.Cu, net GND
- added copper zone on In3.Cu, net GND
- added copper zone on In4.Cu, net GND
- added copper zone on F.Cu, net VDD
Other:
- board text added: "0"
- board text added: "1"
- board text added: "2"
- board text added: "3"
- board text added: "4"
- board text added: "5"
- board text added: "6"
- board text added: "7"
- board text added: "8"
- board text added: "9"
- board text added: "A"
- board text added: "B"
- board text added: "C"
- board text added: "D"
- board text added: "E"
- board text added: "F"
- board text added: "G"
